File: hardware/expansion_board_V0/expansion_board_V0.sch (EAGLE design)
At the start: 215 parts, among them CON7 NC, IC1 DRV8402, IC6 DRV8402, IC7 DRV8402, Q3 25MHz, U14 LAN9514, U8 AM26C32, X10 M1-2, X11 M3-4, X14 M1-2, X15 M3-4, X4 M1-2, X5 M3-4

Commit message: Rework hbridge section and add qei
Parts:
- removed C48, C78, C81: 2.2u, iocene:C_603
- removed C49, C50, C51, C52, C53, C54, C55, C56, C75, C76, C77, C79, C80, C82: 100n, iocene:C_402
- removed C84, C85: 18p, iocene:C_402
- removed C88: NC, iocene:C_402
- removed CON7: NC, iocene:USBUSB3140
- removed J17, J21, J22: (no value), SparkFun-Connectors:M08LONGPADS
- removed L1, L16: 600, iocene:INDUCTANCE_603
- removed L19: NC, iocene:INDUCTANCE_603
- removed Q3: 25MHz, iocene:QUARTZ2
- removed R174, R176, R177, R179, R180, R182: 1k, iocene:R_603
- removed R175, R178, R181: 100, iocene:R_603
- removed R56: 1M, iocene:R_402
- removed R57: 12.4k, iocene:R_402
- removed R58: 12k, iocene:R_402
- removed R64: 10k, iocene:R_402
- removed U14: LAN9514, iocene:LAN9514
- removed U8: AM26C32, iocene:AM26C32
- removed X1, X12, X13, X3, X8, X9: (no value), con-phoenix-254:MPT2
- removed X10, X14, X4: M1-2, con-wago-500:W237-102
- removed X11, X15, X5: M3-4, con-wago-500:W237-102
- added C100, C102, C103, C105, C93, C94, C95, C96, C97, C98, C99: 100n, iocene:C_402
- added C101, C104: 2.2u, iocene:C_603
- added C106, C107: 18p, iocene:C_402
- added C108: NC, iocene:C_402
- added C148, C149, C150, C151, C154, C155, C156, C157, C158: 1u, rcl:C-EUC0805
- added C152, C159: 330u, rcl:CPOL-EUB/3528-21W
- added C153: 47u, rcl:CPOL-EUB/3528-21W
- added C160, C162, C164, C166: 10n, rcl:C-EUC0805
- added C161, C163, C165, C167: 1000u, rcl:CPOL-EUE3.5-10
- added C28, C89: 100n, iocene:C_603
- added C86, C87, C90, C91, C92: 22p, iocene:C_603
- added CON1: NC, iocene:USBUSB3140
- added IC5: DRV8402, etienne:DRV8402
- added L2, L3: 600, iocene:INDUCTANCE_603
- added L4: NC, iocene:INDUCTANCE_603
- added M0, M1, M2, M3, M4, M5: (no value), SparkFun-Connectors:M02-JST-2-PTH-NO_SILK
- added Q1: 25MHz, iocene:QUARTZ2
- added R100, R101, R98, R99: 3.3, rcl:R-EU_R1206
- added R54, R55, R66, R67, R68, R92, R93: 100, iocene:R_603
- added R61, R62, R63, R65, R69, R70, R71, R72, R73, R74, R94, R95, R96, R97: 1k, iocene:R_603
- added R75: 1M, iocene:R_402
- added R76: 12.4k, iocene:R_402
- added R77: 12k, iocene:R_402
- added R78: 10k, iocene:R_402
- added R90, R91: (no value), rcl:R-EU_R0402
- added U1, U2: AM26C32, iocene:AM26C32
- added U3: LAN9514, iocene:LAN9514
- C1, C10, C12, C13, C2, C23, C24, C25, C26, C3, C5, C6: device rcl:C-EUC0805 -> rcl:C-EUC0402
- C11, C14, C15, C16, C18, C30, C44, C45, C46, C7, C8, C9: device rcl:C-EUC0603 -> rcl:C-EUC0402
- C17, C19, C47: device rcl:C-EUC0603K -> rcl:C-EUC0402
- C20: value 100n -> 2.2u
- C21, C22, C27: value 22p -> 100n; device iocene:C_603 -> iocene:C_402
- C31, C32, C33, C34, C35, C38: value 1u -> 100n; device rcl:C-EUC0805 -> rcl:C-EUC0402
- C36: value 330u -> 100n; device rcl:CPOL-EUB/3528-21W -> rcl:C-EUC0402
- C37, C4: value 47u -> 100n; device rcl:CPOL-EUB/3528-21W -> rcl:C-EUC0402
- C57, C58: value 1u -> 22p; device rcl:C-EUC0805 -> iocene:C_603
- C59, C66: value 1u -> 47u; device rcl:C-EUC0805 -> rcl:CPOL-EUB/3528-21W
- C61, C68: value 330u -> 1u; device rcl:CPOL-EUB/3528-21W -> rcl:C-EUC0805
- C62: value 47u -> 1u; device rcl:CPOL-EUB/3528-21W -> rcl:C-EUC0805
- C65: value 1u -> 330u; device rcl:C-EUC0805 -> rcl:CPOL-EUB/3528-21W
- C69, C71: value 10n -> 1u
- C70, C74: value 1000u -> 1u; device rcl:CPOL-EUE3.5-10 -> rcl:C-EUC0805
- C72: value 1000u -> 330u; device rcl:CPOL-EUE3.5-10 -> rcl:CPOL-EUB/3528-21W
- C73: value 10n -> 47u; device rcl:C-EUC0805 -> rcl:CPOL-EUB/3528-21W
- R1, R11, R13, R14, R17, R18, R19, R2, R3: value 0R -> (none); device resistor:R-EU_R0603 -> rcl:R-EU_R0402
- R15, R20, R5: value 1 -> (none); device rcl:R-EU_R0603 -> rcl:R-EU_R0402
- R16, R21, R6: device rcl:R-EU_R0603 -> rcl:R-EU_R0402
- R4, R7, R8: value 3.3 -> (none); device rcl:R-EU_R1206 -> rcl:R-EU_R0402
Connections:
- removed net FAULT2: IC7.FAULT, J21.7
- removed net M1A: C12.1, C25.1, C3.1, IC1.OUT_A, IC6.OUT_A, IC7.OUT_A, X1-1.1, X10-1.KL, X12-1.1, X14-1.KL, X4-1.KL, X8-1.1
- removed net M1C: C1.2, C23.2, C5.2, IC1.OUT_C, IC6.OUT_C, IC7.OUT_C, X11-1.KL, X13-1.1, X15-1.KL, X3-1.1, X5-1.KL, X9-1.1
- removed net N$135: C21.P$2, R174.P$2, U8.A+
- removed net N$136: C22.P$1, R179.P$2, U8.C-
- removed net N$137: C27.P$2, R180.P$2, U8.D+
- removed net N$138: C21.P$1, R176.P$2, U8.A-
- removed net N$139: C22.P$2, R177.P$2, U8.C+
- removed net N$142: C27.P$1, R182.P$2, U8.D-
- removed net N$46: IC6.PWM_D, J17.1
- removed net N$55: C79.P$2, C80.P$2, C81.P$2, U14.VDD18CORE, U14.VDD18CORE@1
- removed net N$56: R58.P$2, U14.USBRBIAS
- removed net N$57: C48.P$2, C49.P$2, L16.2, U14.VDD18USBPLL
- removed net N$600: R64.P$1, U14.NRESET
- removed net N$62: R57.P$2, U14.EXRES
- removed net N$65: C82.P$2, L16.1, U14.VDD18ETHPLL
- removed net N$81: C85.P$2, Q3.2, R56.P$1, U14.XO
- removed net N$82: CON7.D+, U14.USBDP0
- removed net N$89: C88.P$2, CON7.VBUS, L19.2
- removed net N$90: CON7.D-, U14.USBDM0
- removed net N$91: C84.P$2, Q3.1, R56.P$2, U14.XI
- removed net OTW2: IC7.OTW, J21.8
- removed net PWM1_B: IC7.PWM_B, J21.4
- removed net PWM1_C: IC7.PWM_C, J21.3
- removed net PWM1_D: IC7.PWM_D, J21.1
- removed net PWM2_A: IC7.PWM_A, J21.6
- removed net QEI0X: U8.A
- removed net QEI0X+: R174.P$1, R175.P$1
- removed net QEI0X-: R175.P$2, R176.P$1
- removed net RESET1_CD: IC7.RESET_CD, J21.2
- removed net RESET2_AB: IC7.RESET_AB, J21.5
- new net M0_FAULT: IC6.FAULT
- new net M0_OTW: IC6.OTW
- new net M0_PWMA: IC6.PWM_A, IC6.PWM_C
- new net M0_PWMB: IC6.PWM_B, IC6.PWM_D
- new net M0_RST: IC6.RESET_AB, IC6.RESET_CD
- new net M1A2: C14.2, C17.2, IC1.OUT_A, IC1.OUT_B, M1.1
- new net M1A3: C32.2, IC5.OUT_A, M2.1
- new net M1A4: C46.2, IC7.OUT_A, M4.1
- new net M1B3: C26.2, IC5.OUT_B, M2.2
- new net M1B4: C38.2, IC7.OUT_B, M4.2
- new net M1C3: C25.2, IC5.OUT_C, M3.1
- new net M1C4: C37.2, IC7.OUT_C, M5.1
- new net M1D2: C10.2, C13.2, IC1.OUT_C, IC1.OUT_D, M1.2
- new net M1D3: C19.2, IC5.OUT_D, M3.2
- new net M1D4: C34.2, IC7.OUT_D, M5.2
- new net M1_FAULT: IC1.FAULT
- new net M1_OTW: IC1.OTW
- new net M1_PWMA: IC1.PWM_A, IC1.PWM_C
- new net M1_PWMB: IC1.PWM_B, IC1.PWM_D
- new net M1_RST: IC1.RESET_AB, IC1.RESET_CD
- new net M2_FAULT: IC5.FAULT
- new net M2_OTW: IC5.OTW
- new net M2_PWMA: IC5.PWM_A
- new net M2_PWMB: IC5.PWM_B
- new net M2_PWMC: IC5.PWM_C
- new net M2_PWMD: IC5.PWM_D
- new net M2_RST_AB: IC5.RESET_AB
- new net M2_RST_CD: IC5.RESET_CD
- new net M4_FAULT: IC7.FAULT
- new net M4_OTW: IC7.OTW
- new net M4_PWMA: IC7.PWM_A
- new net M4_PWMB: IC7.PWM_B
- new net M4_PWMC: IC7.PWM_C
- new net M4_PWMD: IC7.PWM_D
- new net M4_RST_AB: IC7.RESET_AB
- new net M4_RST_CD: IC7.RESET_CD
- new net N$58: C86.P$1, R62.P$2, U1.C-
- new net N$59: C87.P$2, R63.P$2, U1.D+
- new net N$64: C86.P$2, R61.P$2, U1.C+
- new net N$66: C87.P$1, R65.P$2, U1.D-
- new net N$67: C90.P$2, R69.P$2, U2.A+
- new net N$68: C91.P$1, R72.P$2, U2.C-
- new net N$72: C92.P$2, R73.P$2, U2.D+
- new net N$73: C90.P$1, R70.P$2, U2.A-
- new net N$74: C91.P$2, R71.P$2, U2.C+
- new net N$75: C92.P$1, R74.P$2, U2.D-
- new net N$76: C20.P$2, C21.P$2, L3.2, U3.VDD18USBPLL
- new net N$77: C102.P$2, C103.P$2, C104.P$2, U3.VDD18CORE, U3.VDD18CORE@1
- new net N$78: C105.P$2, L3.1, U3.VDD18ETHPLL
- new net N$79: R76.P$2, U3.EXRES
- new net N$80: R77.P$2, U3.USBRBIAS
- new net N$83: C107.P$2, Q1.2, R75.P$1, U3.XO
- new net N$84: CON1.D+, U3.USBDP0
- new net N$85: C108.P$2, CON1.VBUS, L4.2
- new net N$86: CON1.D-, U3.USBDM0
- new net N$87: R78.P$1, U3.NRESET
- new net N$88: C106.P$2, Q1.1, R75.P$2, U3.XI
- new net QEI1A: U1.C
- new net QEI1A+: R54.P$1, R61.P$1
- new net QEI1A-: R54.P$2, R62.P$1
- new net QEI1B: U1.D
- new net QEI1B+: R55.P$1, R63.P$1
- new net QEI1B-: R55.P$2, R65.P$1
- new net QEI2A: U2.C
- new net QEI2A+: R67.P$1, R71.P$1
- new net QEI2A-: R67.P$2, R72.P$1
- new net QEI2B: U2.D
- new net QEI2B+: R68.P$1, R73.P$1
- new net QEI2B-: R68.P$2, R74.P$1
- new net QEI2X: U2.A
- new net QEI2X+: R66.P$1, R69.P$1
- new net QEI2X-: R66.P$2, R70.P$1
- net 3V3: now also C22.P$2, C27.P$2, C93.P$2, C94.P$2, C95.P$2, L2.1, R78.P$2, U3.AUTOMDIX_EN, U3.NTRST, U3.TEST3, U3.VBUS_DET, U3.VDD33IO, U3.VDD33IO@1, U3.VDD33IO@2, U3.VDD33IO@3, U3.VDD33IO@4; no longer C50.P$2, C51.P$2, C52.P$2, C53.P$2, C54.P$2, L1.1, R64.P$2, U14.AUTOMDIX_EN, U14.NTRST, U14.TEST3, U14.VBUS_DET, U14.VDD33IO, U14.VDD33IO@1, U14.VDD33IO@2, U14.VDD33IO@3, U14.VDD33IO@4
- net 5V: now also C28.P$2, C89.P$2, L4.1, U1.EN+, U1.VCC, U2.EN+, U2.VCC; no longer C20.P$2, L19.1, U8.EN+, U8.VCC
- net ARM_DM: now also U3.USBDM2; no longer U14.USBDM2
- net ARM_DP: now also U3.USBDP2; no longer U14.USBDP2
- net GND: now also C100.P$1, C101.P$1, C102.P$1, C103.P$1, C104.P$1, C105.P$1, C106.P$1, C107.P$1, C108.P$1, C11.2, C12.2, C148.1, C149.1, C15.2, C150.1, C151.1, C152.-, C153.-, C154.1, C155.1, C156.1, C157.1, C158.1, C159.-, C16.2, C160.1, C161.-, C162.1, C163.-, C164.1, C165.-, C166.1, C167.-, C2.2, C21.P$1, C22.P$1, C23.2, C24.2, C27.P$1, C28.P$1, C3.2, C30.2, C31.2, C35.2, C36.2, C44.2, C45.2, C59.-, C6.2, C61.1, C62.1, C65.-, C66.-, C68.1, C7.2, C70.1, C73.-, C74.1, C89.P$1, C93.P$1, C94.P$1, C95.P$1, C96.P$1, C97.P$1, C98.P$1, C99.P$1, CON1.GND, CON1.GND@2, IC5.GND, IC5.GND_A, IC5.GND_B, IC5.GND_C, IC5.GND_D, R14.2, R19.2, R4.2, R6.2, R76.P$1, R77.P$1, U1.EN-, U1.GND, U2.B+, U2.B-, U2.EN-, U2.GND, U3.CLK24_EN, U3.EECS, U3.GND, U3.TEST2; no longer C11.1, C14.1, C15.1, C16.1, C18.1, C30.1, C31.1, C32.1, C33.1, C34.1, C35.1, C36.-, C37.-, C38.1, C4.-, C44.1, C45.1, C46.1, C48.P$1, C49.P$1, C50.P$1, C51.P$1, C52.P$1, C53.P$1, C54.P$1, C55.P$1, C56.P$1, C57.1, C58.1, C59.1, C61.-, C62.-, C65.1, C66.1, C68.-, C7.1, C70.-, C73.1, C74.-, C75.P$1, C76.P$1, C77.P$1, C78.P$1, C79.P$1, C8.1, C80.P$1, C81.P$1, C82.P$1, C84.P$1, C85.P$1, C88.P$1, C9.1, CON7.GND, CON7.GND@2, R15.1, R20.1, R5.1, R57.P$1, R58.P$1, U14.CLK24_EN, U14.EECS, U14.GND, U14.TEST2, U8.B+, U8.B-, U8.EN-, U8.GND
- net GVDD: now also C148.2, C149.2, C150.2, C151.2, C152.+, C153.+, C154.2, C155.2, C156.2, C157.2, C158.2, C159.+, C59.+, C61.2, C62.2, C65.+, C66.+, C68.2, C69.2, C70.2, C71.2, C72.+, C73.+, C74.2, IC5.GVDD_A, IC5.GVDD_B, IC5.GVDD_C, IC5.GVDD_D, IC5.VDD; no longer C31.2, C32.2, C33.2, C34.2, C35.2, C36.+, C37.+, C38.2, C4.+, C57.2, C58.2, C59.2, C61.+, C62.+, C65.2, C66.2, C68.+
- net LAN_3V3: now also C100.P$2, C101.P$2, C96.P$2, C97.P$2, C98.P$2, C99.P$2, L2.2, U3.VDD33A, U3.VDD33A@1, U3.VDD33A@2, U3.VDD33A@3, U3.VDD33A@4, U3.VDD33A@5, U3.VDD33A@6; no longer C55.P$2, C56.P$2, C75.P$2, C76.P$2, C77.P$2, C78.P$2, L1.2, U14.VDD33A, U14.VDD33A@1, U14.VDD33A@2, U14.VDD33A@3, U14.VDD33A@4, U14.VDD33A@5, U14.VDD33A@6
- net M1B: now also C5.2, C8.2, IC6.OUT_A, M0.1; no longer C10.1, C2.1, C24.1, IC1.OUT_B, IC7.OUT_B, X1-2.1, X10-2.KL, X12-2.1, X14-2.KL, X4-2.KL, X8-2.1
- net M1D: now also C1.2, C4.2, IC6.OUT_C, M0.2; no longer C13.2, C26.2, C6.2, IC1.OUT_D, IC7.OUT_D, X11-2.KL, X13-2.1, X15-2.KL, X3-2.1, X5-2.KL, X9-2.1
- net N$1: now also IC1.M1, R7.2; no longer C69.2, R4.1
- net N$107: now also IC7.OC_ADJ, R91.2; no longer C25.2, IC7.BST_A
- net N$108: now also C57.P$2, R94.P$2, U1.A+; no longer C24.2, IC7.BST_B
- net N$109: now also C58.P$1, R97.P$2, U1.B-; no longer C23.1, IC7.BST_C
- net N$110: now also C160.2, R98.1; no longer C26.1, IC7.BST_D
- net N$111: now also C162.2, R99.1; no longer C47.2, IC7.AGND, R11.2, R13.2, R14.2, R15.2, R16.1
- net N$112: now also C164.2, R100.1; no longer C47.1, IC7.VREG
- net N$113: now also C166.2, R101.1; no longer IC7.OC_ADJ, R16.2
- net N$20: now also C17.1, IC1.BST_A; no longer IC1.M1, R19.1
- net N$22: now also C14.1, IC1.BST_B; no longer IC1.M2, R18.1
- net N$24: now also R1.2; no longer R3.1
- net N$25: now also C13.1, IC1.BST_C; no longer IC1.M3, R17.1
- net N$26: now also C10.1, IC1.BST_D; no longer C3.2, IC1.BST_A
- net N$27: now also C18.1, IC1.AGND, R11.1, R13.1, R6.1, R7.1, R8.1; no longer C2.2, IC1.BST_B
- net N$28: now also C18.2, IC1.VREG; no longer C1.1, IC1.BST_C
- net N$3: now also IC1.M2, R8.2; no longer C71.2, R7.1
- net N$30: now also IC1.OC_ADJ, R13.2; no longer C6.1, IC1.BST_D
- net N$32: now also IC5.M1, R15.2; no longer C17.2, IC1.AGND, R17.2, R18.2, R19.2, R20.2, R21.1
- net N$33: now also IC5.M2, R16.2; no longer C17.1, IC1.VREG
- net N$34: now also R2.2; no longer R2.1
- net N$35: now also R3.2; no longer R1.1
- net N$36: now also IC5.M3, R17.2; no longer IC1.OC_ADJ, R21.2
- net N$37: now also C32.1, IC5.BST_A; no longer IC1.OTW, J22.8
- net N$38: now also C26.1, IC5.BST_B; no longer IC6.OTW, J17.8
- net N$39: now also C25.1, IC5.BST_C; no longer IC6.FAULT, J17.7
- net N$4: now also IC1.M3, R11.2; no longer C73.2, R8.1
- net N$40: now also C19.1, IC5.BST_D; no longer IC6.PWM_A, J17.6
- net N$41: now also C33.1, IC5.AGND, R14.1, R15.1, R16.1, R17.1, R18.1; no longer IC1.FAULT, J22.7
- net N$42: now also C33.2, IC5.VREG; no longer IC6.RESET_AB, J17.5
- net N$43: now also IC5.OC_ADJ, R18.2; no longer IC6.PWM_B, J17.4
- net N$44: now also C57.P$1, R95.P$2, U1.A-; no longer IC6.PWM_C, J17.3
- net N$45: now also C58.P$2, R96.P$2, U1.B+; no longer IC6.RESET_CD, J17.2
- net N$47: now also IC7.M1, R20.2; no longer IC1.PWM_A, J22.6
- net N$48: now also C8.1; no longer C12.2
- net N$49: now also C5.1; no longer C10.2
- net N$50: now also IC7.M2, R21.2; no longer IC1.RESET_AB, J22.5
- net N$51: now also IC7.M3, R90.2; no longer IC1.PWM_B, J22.4
- net N$52: now also C46.1, IC7.BST_A; no longer IC1.PWM_C, J22.3
- net N$53: now also C38.1, IC7.BST_B; no longer IC1.RESET_CD, J22.2
- net N$54: now also C37.1, IC7.BST_C; no longer IC1.PWM_D, J22.1
- net N$61: now also C4.1; no longer C5.1
- net N$63: now also C1.1; no longer C13.1
- net N$69: now also C9.1, R1.1, R2.1, R3.1, R4.1, R5.1; no longer C19.2, R1.2, R2.2, R3.2, R5.2, R6.1
- net N$70: now also C9.2; no longer C19.1
- net N$71: now also R5.2; no longer R6.2
- net N$96: now also C34.1, IC7.BST_D; no longer IC7.M1, R14.1
- net N$97: now also C47.1, IC7.AGND, R19.1, R20.1, R21.1, R90.1, R91.1; no longer IC7.M2, R13.1
- net N$98: now also C47.2, IC7.VREG; no longer IC7.M3, R11.1
- net PVDD: now also C11.1, C12.1, C15.1, C16.1, C161.+, C163.+, C165.+, C167.+, C2.1, C23.1, C24.1, C3.1, C30.1, C31.1, C35.1, C36.1, C44.1, C45.1, C6.1, C7.1, IC5.PVDD_A, IC5.PVDD_B, IC5.PVDD_C, IC5.PVDD_D, R100.2, R101.2, R98.2, R99.2; no longer C11.2, C14.2, C15.2, C16.2, C18.2, C30.2, C44.2, C45.2, C46.2, C7.2, C70.+, C72.+, C74.+, C8.2, C9.2, R4.2, R7.2, R8.2
- net QEI0A: now also U1.A; no longer U8.C
- net QEI0A+: now also R92.P$1, R94.P$1; no longer R177.P$1, R178.P$1
- net QEI0A-: now also R92.P$2, R95.P$1; no longer R178.P$2, R179.P$1
- net QEI0B: now also U1.B; no longer U8.D
- net QEI0B+: now also R93.P$1, R96.P$1; no longer R180.P$1, R181.P$1
- net QEI0B-: now also R93.P$2, R97.P$1; no longer R181.P$2, R182.P$1
- net WIFI0_DM: now also U3.USBDM5; no longer U14.USBDM5
- net WIFI0_DP: now also U3.USBDP5; no longer U14.USBDP5
- net WIFI1_DM: now also U3.USBDM3; no longer U14.USBDM3
- net WIFI1_DP: now also U3.USBDP3; no longer U14.USBDP3
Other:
- note added: "GVDD/PVDD - POWER SECTION"
- note added: "H-BRIDGE - CAROUSEL"
- note added: "H-BRIDGE - MOTOR LEFT"
- note added: "H-BRIDGE - MOTOR RIGHT"
- note added: "H-BRIDGE - MOTORS SUPP"
- note added: "MOTOR QEI"
- note added: "POWER SUPPLY"
- note removed: "ETHERNET & USB"
- note removed: "GVDD POWER SECTION:"
- note removed: "H-BRIDGE 1"
- note removed: "H-BRIDGE 2"
- note removed: "H-BRIDGE 3"
- note removed: "PVDD POWER SECTION:"

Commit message: WIP
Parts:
- removed C100, C102, C103, C105, C21, C22, C27, C93, C94, C95, C96, C97, C98, C99: 100n, iocene:C_402
- removed C101, C104, C20: 2.2u, iocene:C_603
- removed C106, C107: 18p, iocene:C_402
- removed C108: NC, iocene:C_402
- removed CON1: NC, iocene:USBUSB3140
- removed J27, J28, J29, J30, J31, J32: (no value), SparkFun-Connectors:M03JST-PTH-VERT
- removed L2, L3: 600, iocene:INDUCTANCE_603
- removed L4: NC, iocene:INDUCTANCE_603
- removed Q1: 25MHz, iocene:QUARTZ2
- removed R75: 1M, iocene:R_402
- removed R76: 12.4k, iocene:R_402
- removed R77: 12k, iocene:R_402
- removed R78: 10k, iocene:R_402
- removed U3: LAN9514, iocene:LAN9514
- added C168, C180, C183: 2.2u, iocene:C_603
- added C169, C170, C171, C172, C173, C174, C175, C176, C177, C178, C179, C181, C182, C184: 100n, iocene:C_402
- added C185, C186: 18p, iocene:C_402
- added C187: NC, iocene:C_402
- added CON2: NC, iocene:USBUSB3140
- added L1, L5: 600, iocene:INDUCTANCE_603
- added L6: NC, iocene:INDUCTANCE_603
- added Q2: 25MHz, iocene:QUARTZ2
- added R136: 1M, iocene:R_402
- added R137: 12.4k, iocene:R_402
- added R138: 12k, iocene:R_402
- added R139: 10k, iocene:R_402
- added U4: LAN9514, iocene:LAN9514
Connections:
- removed net IND_1: J27.1
- removed net IND_2: J28.1
- removed net IND_3: J29.1
- removed net IND_4: J30.1
- removed net IND_5: J31.1
- removed net IND_6: J32.1
- removed net N$76: C20.P$2, C21.P$2, L3.2, U3.VDD18USBPLL
- removed net N$77: C102.P$2, C103.P$2, C104.P$2, U3.VDD18CORE, U3.VDD18CORE@1
- removed net N$78: C105.P$2, L3.1, U3.VDD18ETHPLL
- removed net N$79: R76.P$2, U3.EXRES
- removed net N$80: R77.P$2, U3.USBRBIAS
- removed net N$83: C107.P$2, Q1.2, R75.P$1, U3.XO
- removed net N$84: CON1.D+, U3.USBDP0
- removed net N$85: C108.P$2, CON1.VBUS, L4.2
- removed net N$86: CON1.D-, U3.USBDM0
- removed net N$87: R78.P$1, U3.NRESET
- removed net N$88: C106.P$2, Q1.1, R75.P$2, U3.XI
- removed net QEIA_1: J27.3
- removed net QEIA_2: J28.3
- removed net QEIA_3: J29.3
- removed net QEIA_4: J30.3
- removed net QEIA_5: J31.3
- removed net QEIA_6: J32.3
- removed net QEIB_1: J27.2
- removed net QEIB_2: J28.2
- removed net QEIB_3: J29.2
- removed net QEIB_4: J30.2
- removed net QEIB_5: J31.2
- removed net QEIB_6: J32.2
- new net N$178: C168.P$2, C169.P$2, L5.2, U4.VDD18USBPLL
- new net N$179: C181.P$2, C182.P$2, C183.P$2, U4.VDD18CORE, U4.VDD18CORE@1
- new net N$180: C184.P$2, L5.1, U4.VDD18ETHPLL
- new net N$181: R137.P$2, U4.EXRES
- new net N$182: R138.P$2, U4.USBRBIAS
- new net N$183: C186.P$2, Q2.2, R136.P$1, U4.XO
- new net N$184: CON2.D+, U4.USBDP0
- new net N$185: C187.P$2, CON2.VBUS, L6.2
- new net N$186: CON2.D-, U4.USBDM0
- new net N$187: R139.P$1, U4.NRESET
- new net N$188: C185.P$2, Q2.1, R136.P$2, U4.XI
- net 3V3: now also C170.P$2, C171.P$2, C172.P$2, C173.P$2, C174.P$2, L1.1, R139.P$2, U4.AUTOMDIX_EN, U4.NTRST, U4.TEST3, U4.VBUS_DET, U4.VDD33IO, U4.VDD33IO@1, U4.VDD33IO@2, U4.VDD33IO@3, U4.VDD33IO@4; no longer C22.P$2, C27.P$2, C93.P$2, C94.P$2, C95.P$2, L2.1, R78.P$2, U3.AUTOMDIX_EN, U3.NTRST, U3.TEST3, U3.VBUS_DET, U3.VDD33IO, U3.VDD33IO@1, U3.VDD33IO@2, U3.VDD33IO@3, U3.VDD33IO@4
- net 5V: now also L6.1; no longer L4.1
- net ARM_DM: now also U4.USBDM2; no longer U3.USBDM2
- net ARM_DP: now also U4.USBDP2; no longer U3.USBDP2
- net GND: now also C168.P$1, C169.P$1, C170.P$1, C171.P$1, C172.P$1, C173.P$1, C174.P$1, C175.P$1, C176.P$1, C177.P$1, C178.P$1, C179.P$1, C180.P$1, C181.P$1, C182.P$1, C183.P$1, C184.P$1, C185.P$1, C186.P$1, C187.P$1, CON2.GND, CON2.GND@2, R137.P$1, R138.P$1, U4.CLK24_EN, U4.EECS, U4.GND, U4.TEST2; no longer C100.P$1, C101.P$1, C102.P$1, C103.P$1, C104.P$1, C105.P$1, C106.P$1, C107.P$1, C108.P$1, C20.P$1, C21.P$1, C22.P$1, C27.P$1, C93.P$1, C94.P$1, C95.P$1, C96.P$1, C97.P$1, C98.P$1, C99.P$1, CON1.GND, CON1.GND@2, R76.P$1, R77.P$1, U3.CLK24_EN, U3.EECS, U3.GND, U3.TEST2
- net LAN_3V3: now also C175.P$2, C176.P$2, C177.P$2, C178.P$2, C179.P$2, C180.P$2, L1.2, U4.VDD33A, U4.VDD33A@1, U4.VDD33A@2, U4.VDD33A@3, U4.VDD33A@4, U4.VDD33A@5, U4.VDD33A@6; no longer C100.P$2, C101.P$2, C96.P$2, C97.P$2, C98.P$2, C99.P$2, L2.2, U3.VDD33A, U3.VDD33A@1, U3.VDD33A@2, U3.VDD33A@3, U3.VDD33A@4, U3.VDD33A@5, U3.VDD33A@6
- net WIFI0_DM: now also U4.USBDM5; no longer U3.USBDM5
- net WIFI0_DP: now also U4.USBDP5; no longer U3.USBDP5
- net WIFI1_DM: now also U4.USBDM3; no longer U3.USBDM3
- net WIFI1_DP: now also U4.USBDP3; no longer U3.USBDP3
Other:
- note added: "USB - WiFi"
- note removed: "QEIs"

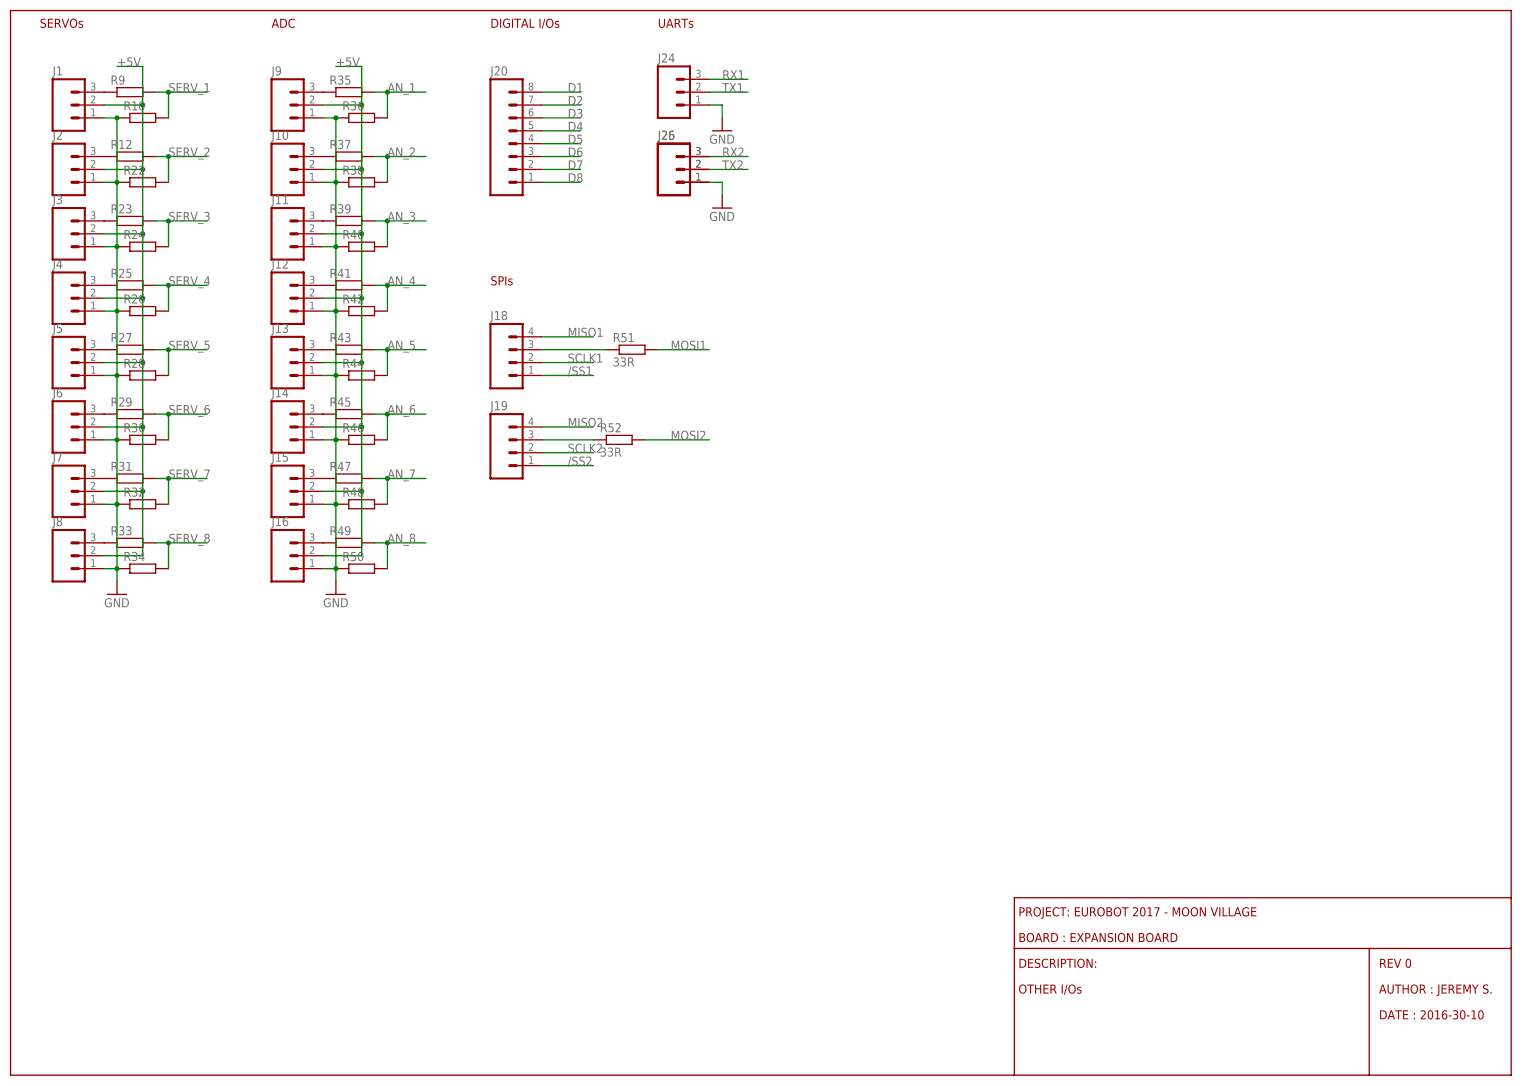
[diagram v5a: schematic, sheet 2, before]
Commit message: Add logic level translator, missing I2C and UART
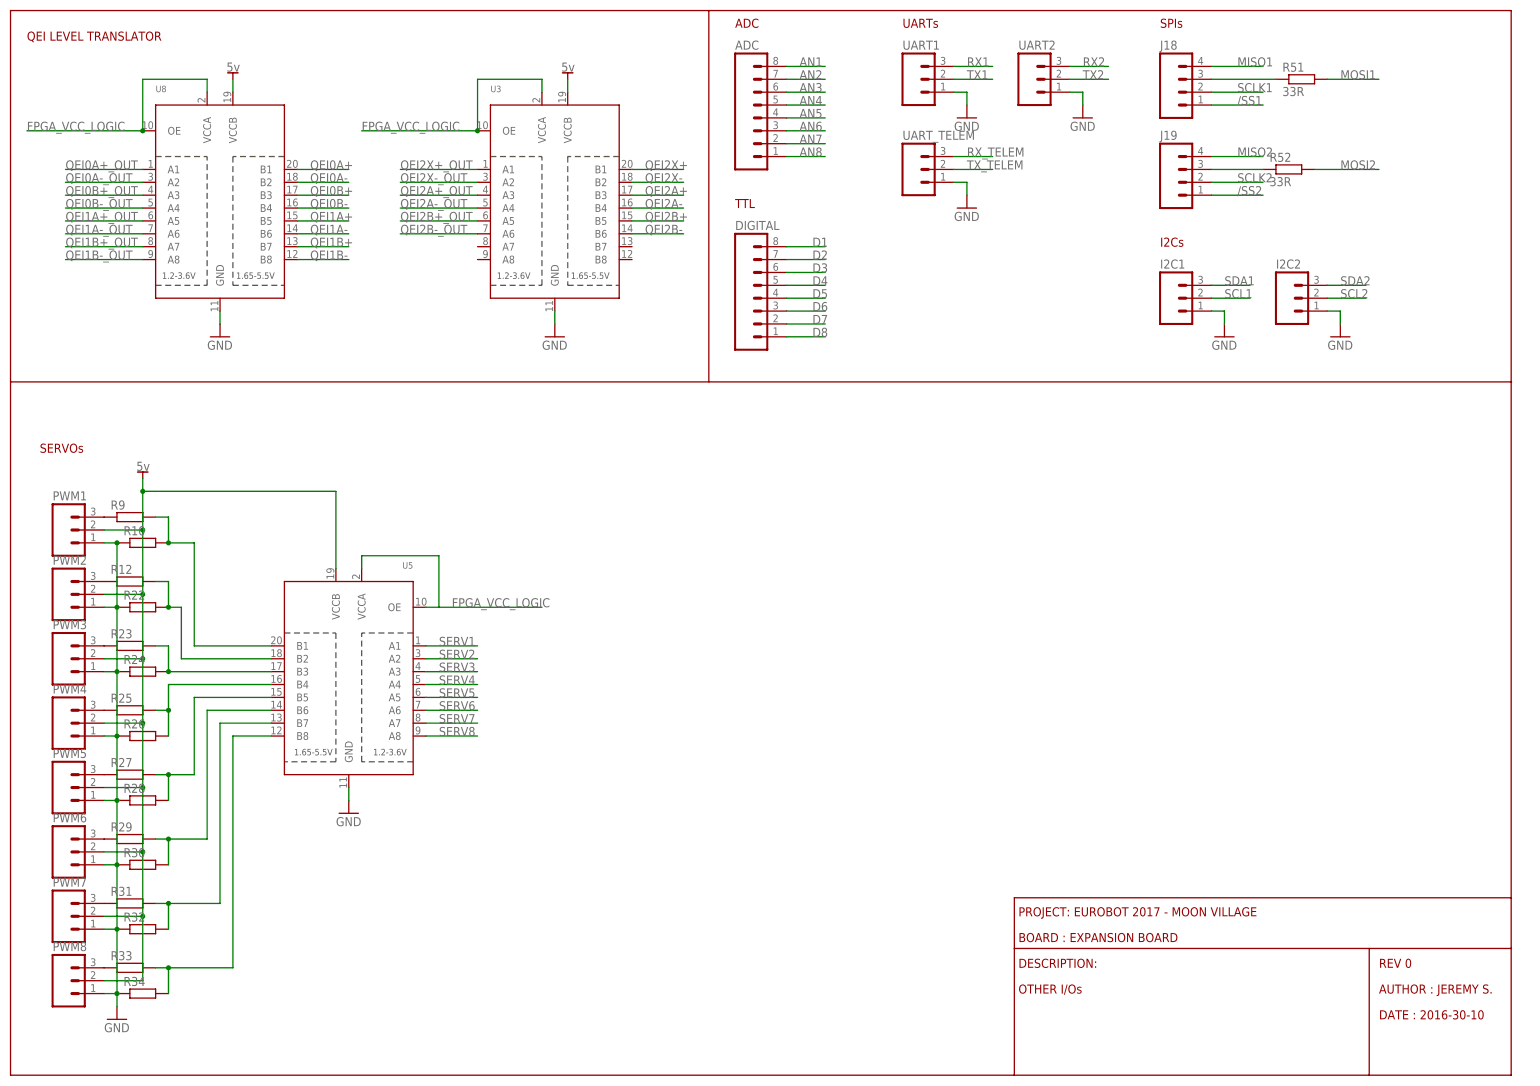
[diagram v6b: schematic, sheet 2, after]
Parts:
- removed J1, J10, J11, J12, J13, J14, J15, J16, J2, J24, J25, J26, J3, J4, J5, J6, J7, J8, J9: (no value), SparkFun-Connectors:M03LONGPADS
- removed J20: (no value), SparkFun-Connectors:M08LONGPADS
- removed R35, R36, R37, R38, R39, R40, R41, R42, R43, R44, R45, R46, R47, R48, R49, R50: (no value), resistor:R-EU_R0603
- added ADC, DIGITAL: (no value), SparkFun-Connectors:M08LONGPADS
- added I2C1, I2C2, PWM1, PWM2, PWM3, PWM4, PWM5, PWM6, PWM7, PWM8, UART1, UART2, UART_TELEM: (no value), SparkFun-Connectors:M03LONGPADS
- added U3, U5, U8: (no value), adafruit:TXB0108PWR
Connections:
- removed net AN_1: R35.2, R36.2
- removed net AN_2: R37.2, R38.2
- removed net AN_3: R39.2, R40.2
- removed net AN_4: R41.2, R42.2
- removed net AN_5: R43.2, R44.2
- removed net AN_6: R45.2, R46.2
- removed net AN_7: R47.2, R48.2
- removed net AN_8: R49.2, R50.2
- removed net N$10: J12.3, R41.1
- removed net N$12: J13.3, R43.1
- removed net N$14: J14.3, R45.1
- removed net N$16: J15.3, R47.1
- removed net N$18: J16.3, R49.1
- removed net N$2: J9.3, R35.1
- removed net N$7: J10.3, R37.1
- removed net N$8: J11.3, R39.1
- new net AN1: ADC.8
- new net AN2: ADC.7
- new net AN3: ADC.6
- new net AN4: ADC.5
- new net AN5: ADC.4
- new net AN6: ADC.3
- new net AN7: ADC.2
- new net AN8: ADC.1
- new net FPGA_VCC_LOGIC: U3.OE, U3.VCCA, U5.OE, U5.VCCA, U8.OE, U8.VCCA
- new net QEI0A+_OUT: U8.A1
- new net QEI0A-_OUT: U8.A2
- new net QEI0B+_OUT: U8.A3
- new net QEI0B-_OUT: U8.A4
- new net QEI1A+_OUT: U8.A5
- new net QEI1A-_OUT: U8.A6
- new net QEI1B+_OUT: U8.A7
- new net QEI1B-_OUT: U8.A8
- new net QEI2A+_OUT: U3.A3
- new net QEI2A-_OUT: U3.A4
- new net QEI2B+_OUT: U3.A5
- new net QEI2B-_OUT: U3.A6
- new net QEI2X+_OUT: U3.A1
- new net QEI2X-_OUT: U3.A2
- new net RX_TELEM: UART_TELEM.3
- new net SCL1: I2C1.2
- new net SCL2: I2C2.2
- new net SDA1: I2C1.3
- new net SDA2: I2C2.3
- new net SERV1: U5.A1
- new net SERV2: U5.A2
- new net SERV3: U5.A3
- new net SERV4: U5.A4
- new net SERV5: U5.A5
- new net SERV6: U5.A6
- new net SERV7: U5.A7
- new net SERV8: U5.A8
- new net TX_TELEM: UART_TELEM.2
- net +5V: no longer J1.2, J10.2, J11.2, J12.2, J13.2, J14.2, J15.2, J16.2, J2.2, J3.2, J4.2, J5.2, J6.2, J7.2, J8.2, J9.2
- net 5V: now also PWM1.2, PWM2.2, PWM3.2, PWM4.2, PWM5.2, PWM6.2, PWM7.2, PWM8.2, U3.VCCB, U5.VCCB, U8.VCCB
- net D1: now also DIGITAL.8; no longer J20.8
- net D2: now also DIGITAL.7; no longer J20.7
- net D3: now also DIGITAL.6; no longer J20.6
- net D4: now also DIGITAL.5; no longer J20.5
- net D5: now also DIGITAL.4; no longer J20.4
- net D6: now also DIGITAL.3; no longer J20.3
- net D7: now also DIGITAL.2; no longer J20.2
- net D8: now also DIGITAL.1; no longer J20.1
- net GND: now also I2C1.1, I2C2.1, PWM1.1, PWM2.1, PWM3.1, PWM4.1, PWM5.1, PWM6.1, PWM7.1, PWM8.1, U3.GND, U5.GND, U8.GND, UART1.1, UART2.1, UART_TELEM.1; no longer J1.1, J10.1, J11.1, J12.1, J13.1, J14.1, J15.1, J16.1, J2.1, J24.1, J25.1, J26.1, J3.1, J4.1, J5.1, J6.1, J7.1, J8.1, J9.1, R36.1, R38.1, R40.1, R42.1, R44.1, R46.1, R48.1, R50.1
- net N$11: now also PWM2.3; no longer J2.3
- net N$13: now also PWM3.3; no longer J3.3
- net N$15: now also PWM4.3; no longer J4.3
- net N$17: now also PWM5.3; no longer J5.3
- net N$19: now also PWM6.3; no longer J6.3
- net N$29: now also PWM7.3; no longer J7.3
- net N$31: now also PWM8.3; no longer J8.3
- net N$9: now also PWM1.3; no longer J1.3
- net QEI0A+: now also U8.B1
- net QEI0A-: now also U8.B2
- net QEI0B+: now also U8.B3
- net QEI0B-: now also U8.B4
- net QEI1A+: now also U8.B5
- net QEI1A-: now also U8.B6
- net QEI1B+: now also U8.B7
- net QEI1B-: now also U8.B8
- net QEI2A+: now also U3.B3
- net QEI2A-: now also U3.B4
- net QEI2B+: now also U3.B5
- net QEI2B-: now also U3.B6
- net QEI2X+: now also U3.B1
- net QEI2X-: now also U3.B2
- net RX1: now also UART1.3; no longer J24.3
- net RX2: now also UART2.3; no longer J25.3, J26.3
- net SERV_1: now also U5.B1
- net SERV_2: now also U5.B2
- net SERV_3: now also U5.B3
- net SERV_4: now also U5.B4
- net SERV_5: now also U5.B5
- net SERV_6: now also U5.B6
- net SERV_7: now also U5.B7
- net SERV_8: now also U5.B8
- net TX1: now also UART1.2; no longer J24.2
- net TX2: now also UART2.2; no longer J25.2, J26.2
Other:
- note added: "I2Cs"
- note added: "QEI LEVEL TRANSLATOR"
- note added: "TTL"
- note removed: "DIGITAL I/Os"
- moved on the sheet: C28, C89, J18, J19, R10, R12, R22, R23, R24, R25, R26, R27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
